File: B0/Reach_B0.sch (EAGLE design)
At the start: 179 parts, among them IC1 TMC2100-LA, IC10 74AHC1G126DCK, IC11 74AHC1G126DCK, IC18 74AHC1G126DCK, IC2 TMC2100-LA, IC3 74AHC1G126DCK, IC4 74AHC1G126DCK, IC5 74AHC1G126DCK, IC6 74AHC1G126DCK, IC7 74AHC1G126DCK, IC8 TMC2100-LA, IC9 74AHC1G126DCK, P8 F-2X23-, P9 F-2X23-, Q2 AON6758, Q3 AON6758, U1 SN74AHC595PW, U10 RT8268, U11 PCA9685PW, U18 CAT24C256, U2 SN74AHC595PW, U3 MCP9600, U4 MCP9600, U5 MCP9600, U6 MCP9600, U7 SN74AHC595PW, X1 22-05-7028-02, X11 22-05-7028-02, X14 22-05-7048-04, X2 MSTBA4, X21 MSTBA2, X3 MSTBA2, X4 22-05-7028-02, X5 22-05-7028-02, X6 22-05-7048-04, X7 22-05-7028-02, X8 22-05-7048-04, X9 22-05-7028-02

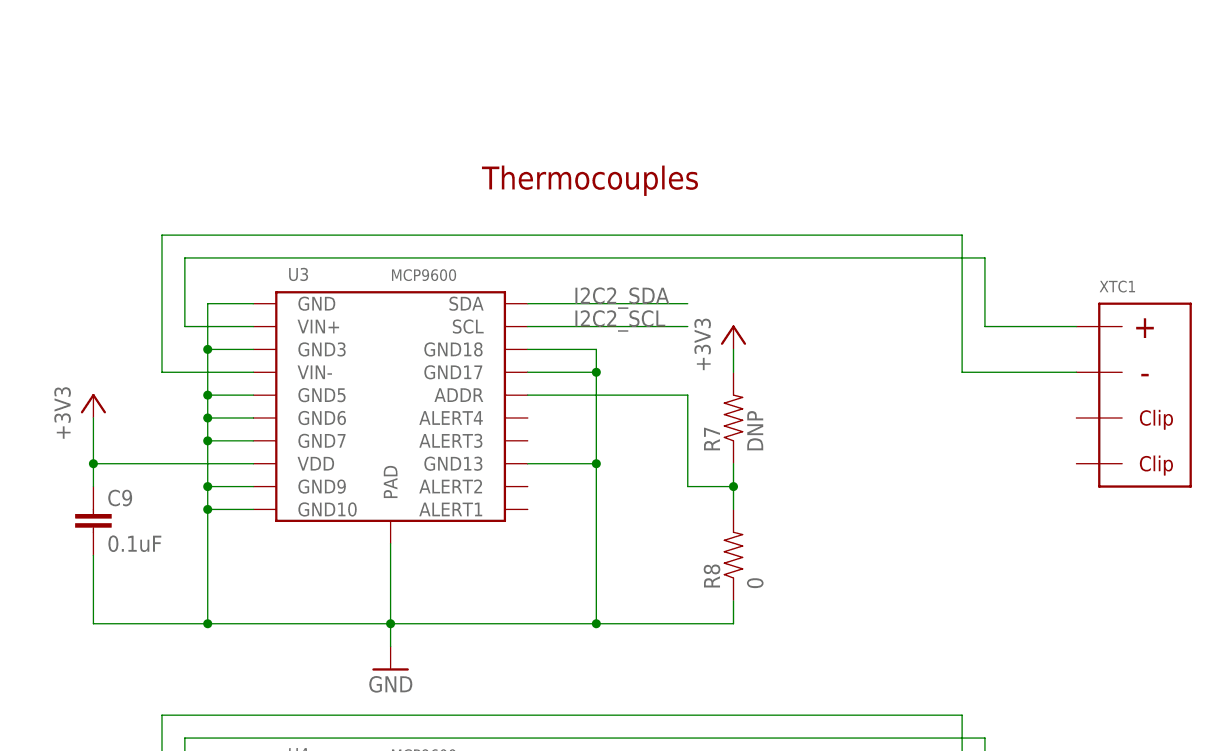
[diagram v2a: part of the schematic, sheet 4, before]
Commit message: example layout of esd and low pass filter added to thermocouple1
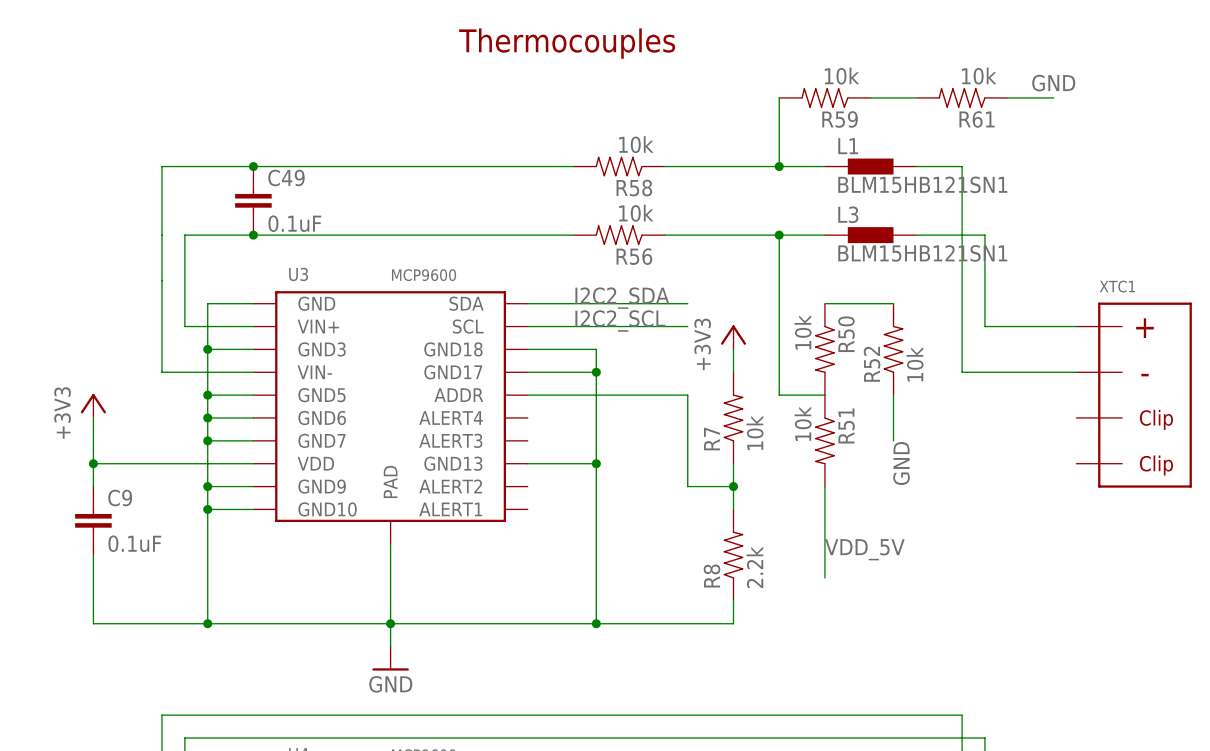
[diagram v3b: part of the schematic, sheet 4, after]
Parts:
- added C49: 0.1uF, rcl:C-EUC0402
- added L1, L3: BLM15HB121SN1, inductors:BLM15HB121SN1
- added R50, R51, R52, R56, R58, R59, R61: 10k, SparkFun-Resistors:RESISTOR0402-RES
- R7: value DNP -> 10k
- R8: value 0 -> 2.2k
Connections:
- new net N$11: L3.1, R50.2, R51.1, R56.1
- new net N$51: R50.1, R52.2
- new net N$70: C49.2, R56.2, U3.VIN+
- new net N$71: C49.1, R58.2, U3.VIN-
- new net N$72: L1.1, R58.1, R59.2
- new net N$73: R59.1, R61.2
- net GND: now also R52.1, R61.1
- net N$14: now also L3.2; no longer U3.VIN+
- net N$15: now also L1.2; no longer U3.VIN-
- net VDD_5V: now also R51.2
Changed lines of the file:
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@@
 <?xml version="1.0" encoding="utf-8"?>
 <!DOCTYPE eagle SYSTEM "eagle.dtd">
-<eagle version="8.0.2">
+<eagle version="8.0.1">
 <drawing>
 <settings>
@@
 <part name="GND12" library="supply1" deviceset="GND" device=""/>
 <part name="+3V8" library="supply1" deviceset="+3V3" device=""/>
-<part name="R7" library="SparkFun-Resistors" deviceset="RESISTOR" device="0402-RES" value="DNP"/>
-<part name="R8" library="SparkFun-Resistors" deviceset="RESISTOR" device="0402-RES" value="0"/>
+<part name="R7" library="SparkFun-Resistors" deviceset="RESISTOR" device="0402-RES" value="10k"/>
+<part name="R8" library="SparkFun-Resistors" deviceset="RESISTOR" device="0402-RES" value="2.2k"/>
 <part name="+3V10" library="supply1" deviceset="+3V3" device=""/>
 <part name="XTC2" library="reach_custom" deviceset="NEWPORT_THERMOCOUPLE_CONNECTOR" device="PCC-SMP-V"/>
@@
 <attribute name="MPN" value="RHS1V101MCN1GS"/>
 </part>
+<part name="C49" library="rcl" deviceset="C-EU" device="C0402" value="0.1uF"/>
+<part name="R50" library="SparkFun-Resistors" deviceset="RESISTOR" device="0402-RES" value="10k"/>
+<part name="R51" library="SparkFun-Resistors" deviceset="RESISTOR" device="0402-RES" value="10k"/>
+<part name="R52" library="SparkFun-Resistors" deviceset="RESISTOR" device="0402-RES" value="10k"/>
+<part name="R56" library="SparkFun-Resistors" deviceset="RESISTOR" device="0402-RES" value="10k"/>
+<part name="R58" library="SparkFun-Resistors" deviceset="RESISTOR" device="0402-RES" value="10k"/>
+<part name="R59" library="SparkFun-Resistors" deviceset="RESISTOR" device="0402-RES" value="10k"/>
+<part name="R61" library="SparkFun-Resistors" deviceset="RESISTOR" device="0402-RES" value="10k"/>
+<part name="L1" library="inductors" deviceset="BLM15H" device="" technology="B121SN1"/>
+<part name="L3" library="inductors" deviceset="BLM15H" device="" technology="B121SN1"/>
 </parts>
 <sheets>
@@
 <text x="63.5" y="127" size="2.54" layer="94" font="vector" ratio="15">PWM extension</text>
 <text x="93.98" y="233.68" size="2.54" layer="94" font="vector" ratio="15" rot="MR0">Thermistors</text>
-<text x="289.56" y="236.22" size="2.54" layer="94" font="vector" ratio="15">Thermocouples</text>
+<text x="287.02" y="251.46" size="2.54" layer="94" font="vector" ratio="15">Thermocouples</text>
 </plain>
 <instances>
@@
 <instance part="C29" gate="G$1" x="246.38" y="93.98"/>
 <instance part="C30" gate="G$1" x="246.38" y="40.64"/>
+<instance part="C49" gate="G$1" x="264.16" y="236.22"/>
+<instance part="R50" gate="G$1" x="327.66" y="218.44" rot="R270"/>
+<instance part="R51" gate="G$1" x="327.66" y="208.28" rot="R270"/>
+<instance part="R52" gate="G$1" x="335.28" y="218.44" rot="R90"/>
+<instance part="R56" gate="G$1" x="304.8" y="231.14" rot="R180"/>
+<instance part="R58" gate="G$1" x="304.8" y="238.76" rot="R180"/>
+<instance part="R59" gate="G$1" x="327.66" y="246.38" rot="R180"/>
+<instance part="R61" gate="G$1" x="342.9" y="246.38" rot="R180"/>
+<instance part="L1" gate="G$1" x="332.74" y="238.76"/>
+<instance part="L3" gate="G$1" x="332.74" y="231.14"/>
 </instances>
 <busses>
@@
 <junction x="259.08" y="27.94"/>
 </segment>
+<segment>
+<pinref part="R52" gate="G$1" pin="1"/>
+<wire x1="335.28" y1="213.36" x2="335.28" y2="208.28" width="0.1524" layer="91"/>
+<label x="335.28" y="208.28" size="1.778" layer="95" rot="R270"/>
+</segment>
+<segment>
+<pinref part="R61" gate="G$1" pin="1"/>
+<wire x1="347.98" y1="246.38" x2="353.06" y2="246.38" width="0.1524" layer="91"/>
+<label x="355.6" y="248.92" size="1.778" layer="95" rot="R180"/>
+</segment>
 </net>
 <net name="I2C2_SCL" class="0">
@@
 <label x="35.56" y="91.44" size="1.778" layer="95" rot="R180" xref="yes"/>
 </segment>
+<segment>
+<pinref part="R51" gate="G$1" pin="2"/>
+<wire x1="327.66" y1="203.2" x2="327.66" y2="193.04" width="0.1524" layer="91"/>
+<label x="327.66" y="195.58" size="1.778" layer="95"/>
+</segment>
 </net>
 <net name="HEATER_B" class="0">
@@
 </segment>
 </net>
-<net name="N$14" class="0">
-<segment>
-<pinref part="U3" gate="G$1" pin="VIN+"/>
-<wire x1="264.16" y1="220.98" x2="256.54" y2="220.98" width="0.1524" layer="91"/>
-<wire x1="256.54" y1="220.98" x2="256.54" y2="228.6" width="0.1524" layer="91"/>
-<wire x1="256.54" y1="228.6" x2="345.44" y2="228.6" width="0.1524" layer="91"/>
-<wire x1="345.44" y1="228.6" x2="345.44" y2="220.98" width="0.1524" layer="91"/>
-<pinref part="XTC1" gate="G$1" pin="P$1"/>
-<wire x1="345.44" y1="220.98" x2="355.6" y2="220.98" width="0.1524" layer="91"/>
-</segment>
-</net>
 <net name="N$15" class="0">
 <segment>
-<pinref part="U3" gate="G$1" pin="VIN-"/>
-<wire x1="264.16" y1="215.9" x2="254" y2="215.9" width="0.1524" layer="91"/>
-<wire x1="254" y1="215.9" x2="254" y2="231.14" width="0.1524" layer="91"/>
-<wire x1="254" y1="231.14" x2="342.9" y2="231.14" width="0.1524" layer="91"/>
-<wire x1="342.9" y1="231.14" x2="342.9" y2="215.9" width="0.1524" layer="91"/>
+<wire x1="342.9" y1="238.76" x2="342.9" y2="215.9" width="0.1524" layer="91"/>
 <pinref part="XTC1" gate="G$1" pin="P$2"/>
 <wire x1="342.9" y1="215.9" x2="355.6" y2="215.9" width="0.1524" layer="91"/>
+<wire x1="337.82" y1="238.76" x2="342.9" y2="238.76" width="0.1524" layer="91"/>
+<pinref part="L1" gate="G$1" pin="2"/>
 </segment>
 </net>
@@
 </segment>
 </net>
+<net name="N$11" class="0">
+<segment>
+<pinref part="R51" gate="G$1" pin="1"/>
+<pinref part="R50" gate="G$1" pin="2"/>
+<wire x1="327.66" y1="213.36" x2="322.58" y2="213.36" width="0.1524" layer="91"/>
+<pinref part="R56" gate="G$1" pin="1"/>
+<wire x1="309.88" y1="231.14" x2="322.58" y2="231.14" width="0.1524" layer="91"/>
+<wire x1="322.58" y1="231.14" x2="327.66" y2="231.14" width="0.1524" layer="91"/>
+<wire x1="322.58" y1="213.36" x2="322.58" y2="231.14" width="0.1524" layer="91"/>
+<junction x="322.58" y="231.14"/>
+<pinref part="L3" gate="G$1" pin="1"/>
+</segment>
+</net>
+<net name="N$51" class="0">
+<segment>
+<pinref part="R52" gate="G$1" pin="2"/>
+<pinref part="R50" gate="G$1" pin="1"/>
+<wire x1="335.28" y1="223.52" x2="327.66" y2="223.52" width="0.1524" layer="91"/>
+</segment>
+</net>
+<net name="N$70" class="0">
+<segment>
+<pinref part="U3" gate="G$1" pin="VIN+"/>
+<wire x1="264.16" y1="220.98" x2="256.54" y2="220.98" width="0.1524" layer="91"/>
+<wire x1="256.54" y1="220.98" x2="256.54" y2="231.14" width="0.1524" layer="91"/>
+<pinref part="R56" gate="G$1" pin="2"/>
+<wire x1="256.54" y1="231.14" x2="264.16" y2="231.14" width="0.1524" layer="91"/>
+<pinref part="C49" gate="G$1" pin="2"/>
+<wire x1="264.16" y1="231.14" x2="299.72" y2="231.14" width="0.1524" layer="91"/>
+<junction x="264.16" y="231.14"/>
+</segment>
+</net>
+<net name="N$71" class="0">
+<segment>
+<pinref part="U3" gate="G$1" pin="VIN-"/>
+<wire x1="264.16" y1="215.9" x2="254" y2="215.9" width="0.1524" layer="91"/>
+<wire x1="254" y1="215.9" x2="254" y2="226.06" width="0.1524" layer="91"/>
+<pinref part="R58" gate="G$1" pin="2"/>
+<wire x1="254" y1="226.06" x2="254" y2="231.14" width="0.1524" layer="91"/>
+<wire x1="299.72" y1="238.76" x2="264.16" y2="238.76" width="0.1524" layer="91"/>
+<wire x1="264.16" y1="238.76" x2="254" y2="238.76" width="0.1524" layer="91"/>
+<wire x1="254" y1="238.76" x2="254" y2="231.14" width="0.1524" layer="91"/>
+<pinref part="C49" gate="G$1" pin="1"/>
+<junction x="264.16" y="238.76"/>
+</segment>
+</net>
+<net name="N$73" class="0">
+<segment>
+<pinref part="R61" gate="G$1" pin="2"/>
+<pinref part="R59" gate="G$1" pin="1"/>
+<wire x1="337.82" y1="246.38" x2="332.74" y2="246.38" width="0.1524" layer="91"/>
+</segment>
+</net>
+<net name="N$14" class="0">
+<segment>
+<pinref part="XTC1" gate="G$1" pin="P$1"/>
+<pinref part="L3" gate="G$1" pin="2"/>
+<wire x1="337.82" y1="231.14" x2="345.44" y2="231.14" width="0.1524" layer="91"/>
+<wire x1="345.44" y1="231.14" x2="345.44" y2="220.98" width="0.1524" layer="91"/>
+<wire x1="345.44" y1="220.98" x2="355.6" y2="220.98" width="0.1524" layer="91"/>
+</segment>
+</net>
+<net name="N$72" class="0">
+<segment>
+<pinref part="L1" gate="G$1" pin="1"/>
+<wire x1="322.58" y1="238.76" x2="327.66" y2="238.76" width="0.1524" layer="91"/>
+<pinref part="R59" gate="G$1" pin="2"/>
+<wire x1="322.58" y1="246.38" x2="322.58" y2="238.76" width="0.1524" layer="91"/>
+<junction x="322.58" y="238.76"/>
+<pinref part="R58" gate="G$1" pin="1"/>
+<wire x1="309.88" y1="238.76" x2="322.58" y2="238.76" width="0.1524" layer="91"/>
+</segment>
+</net>

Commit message: supply layout complete
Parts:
- removed R50, R51, R52, R59, R61: 10k, SparkFun-Resistors:RESISTOR0402-RES
- R56, R58: value 10k -> 100
- R7: value 10k -> DNP
- R8: value 2.2k -> 0
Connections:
- removed net N$51: R50.1, R52.2
- removed net N$73: R59.1, R61.2
- removed net N$9: C17.1, U11.VDD
- new net SER_3: U2.QH_2, U7.SER
- net GND: no longer R52.1, R61.1
- net N$11: no longer R50.2, R51.1
- net N$72: no longer R59.2
- net SER_2: now also U2.SER; no longer U2.QH_2, U7.QH_2
- net SPI1_MOSI: no longer U2.SER, U7.SER
- net VDD_5V: now also C17.1, U11.VDD; no longer R51.2
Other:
- moved on the sheet: C81, L1, L3, R56, R58
